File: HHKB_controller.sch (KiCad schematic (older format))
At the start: 34 parts, among them CN1 JP, CN2 PRO2, J1 USB_mini_micro_B, P1 GND, P2 D+, P3 D-, P4 VUSB, P5 PD1, P6 PD0, P7 GND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

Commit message: Add current measure pins and change pin pad size
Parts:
- added P10, P11, P9: CONN_1, keyboard_parts:PIN_1, symbol CONN_1
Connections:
- wire segments 153 -> 155
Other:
- note added: "Current measure"
- note added: "Current mesure"
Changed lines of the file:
@@
 	-1   0    0    1
 $EndComp
-Text Notes 900  3000 0    60   Italic 0
+Text Notes 900  3100 0    60   Italic 0
 USB pinouts for external connector
 Text Notes 4350 2200 0    60   Italic 0
@@
 	1    0    0    -1
 $EndComp
+$Comp
+L CONN_1 P10
+U 1 1 5485F22B
+P 2875 5450
+F 0 "P10" H 2955 5450 40  0000 L CNN
+F 1 "CONN_1" H 2875 5505 30  0001 C CNN
+F 2 "keyboard_parts:PIN_1" H 2875 5450 60  0001 C CNN
+F 3 "" H 2875 5450 60  0000 C CNN
+	1    2875 5450
+	0    -1   -1   0
+$EndComp
+$Comp
+L CONN_1 P9
+U 1 1 5485F339
+P 2775 5450
+F 0 "P9" H 2855 5450 40  0000 L CNN
+F 1 "CONN_1" H 2775 5505 30  0001 C CNN
+F 2 "keyboard_parts:PIN_1" H 2775 5450 60  0001 C CNN
+F 3 "" H 2775 5450 60  0000 C CNN
+	1    2775 5450
+	0    -1   -1   0
+$EndComp
+Text Notes 2475 5250 0    60   ~ 0
+Current mesure
+Connection ~ 2875 5600
+Connection ~ 2775 5600
+$Comp
+L CONN_1 P11
+U 1 1 54865141
+P 1150 2925
+F 0 "P11" H 1230 2925 40  0000 L CNN
+F 1 "CONN_1" H 1150 2980 30  0001 C CNN
+F 2 "keyboard_parts:PIN_1" H 1150 2925 60  0001 C CNN
+F 3 "" H 1150 2925 60  0000 C CNN
+	1    1150 2925
+	-1   0    0    1
+$EndComp
+Wire Wire Line
+	1300 2925 1375 2925
+Wire Wire Line
+	1375 2925 1375 2825
+Connection ~ 1375 2825
+Text Notes 1475 2950 0    60   ~ 0
+Current measure
 $EndSCHEMATC

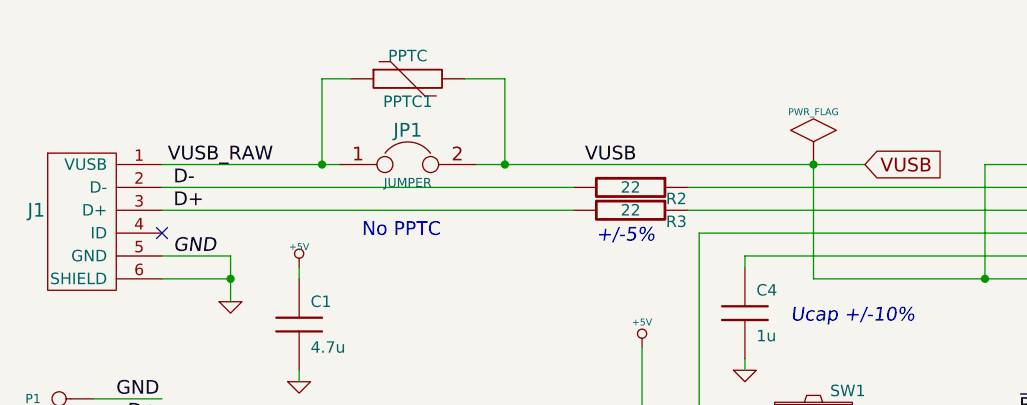
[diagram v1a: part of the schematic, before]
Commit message: Remove solder jumper for Polyfuse
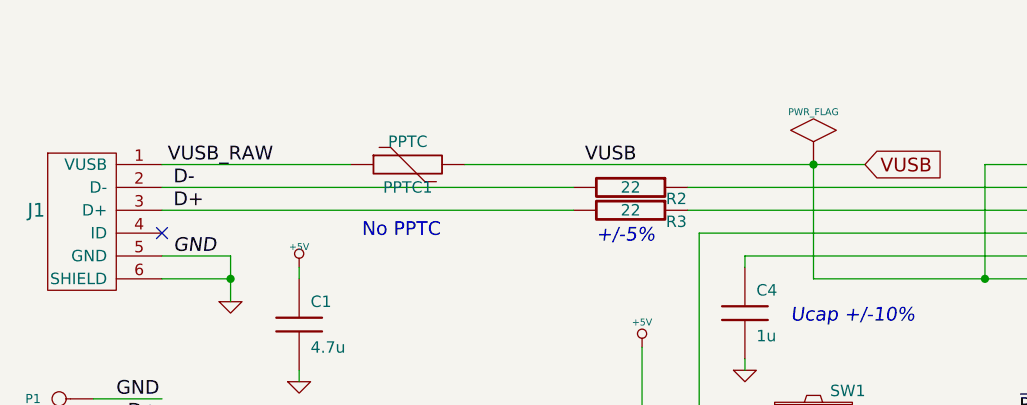
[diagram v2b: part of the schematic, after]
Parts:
- removed JP1: JUMPER, keyboard_parts:SOLDER_JUMPER_2, symbol JUMPER
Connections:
- wire segments 155 -> 151
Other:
- moved on the sheet: PPTC1
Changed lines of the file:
@@
 LIBS:keyboard_parts
 LIBS:HHKB_controller-cache
-EELAYER 24 0
+EELAYER 25 0
 EELAYER END
 $Descr A4 11693 8268
@@
 L PPTC PPTC1
 U 1 1 5417AF4F
-P 2675 1125
-F 0 "PPTC1" H 2675 1225 50  0000 C CNN
-F 1 "PPTC" H 2675 1025 50  0000 C CNN
-F 2 "keyboard_parts:PPTC_nano" V 2675 1125 60  0001 C CNN
-F 3 "" V 2675 1125 60  0000 C CNN
-	1    2675 1125
+P 2675 1500
+F 0 "PPTC1" H 2675 1600 50  0000 C CNN
+F 1 "PPTC" H 2675 1400 50  0000 C CNN
+F 2 "keyboard_parts:PPTC_nano" V 2675 1500 60  0001 C CNN
+F 3 "" V 2675 1500 60  0000 C CNN
+	1    2675 1500
 	1    0    0    1
-$EndComp
-$Comp
-L JUMPER JP1
-U 1 1 5417AF56
-P 2675 1500
-F 0 "JP1" H 2675 1650 60  0000 C CNN
-F 1 "JUMPER" H 2675 1420 40  0000 C CNN
-F 2 "keyboard_parts:SOLDER_JUMPER_2" H 2675 1500 60  0001 C CNN
-F 3 "" H 2675 1500 60  0000 C CNN
-	1    2675 1500
-	1    0    0    -1
 $EndComp
 Text Label 3450 1500 0    60   ~ 0
@@
 	5650 1700 3900 1700
 Wire Wire Line
-	1600 1500 2375 1500
-Wire Wire Line
-	2975 1500 4675 1500
-Wire Wire Line
-	2425 1125 2300 1125
-Wire Wire Line
-	2300 1125 2300 1500
-Connection ~ 2300 1500
-Wire Wire Line
-	2925 1125 3100 1125
-Wire Wire Line
-	3100 1125 3100 1500
-Connection ~ 3100 1500
+	1600 1500 2425 1500
 Wire Wire Line
 	5200 1500 5200 2000
@@
 Text Notes 1475 2950 0    60   ~ 0
 Current measure
+Wire Wire Line
+	2925 1500 4675 1500
 $EndSCHEMATC

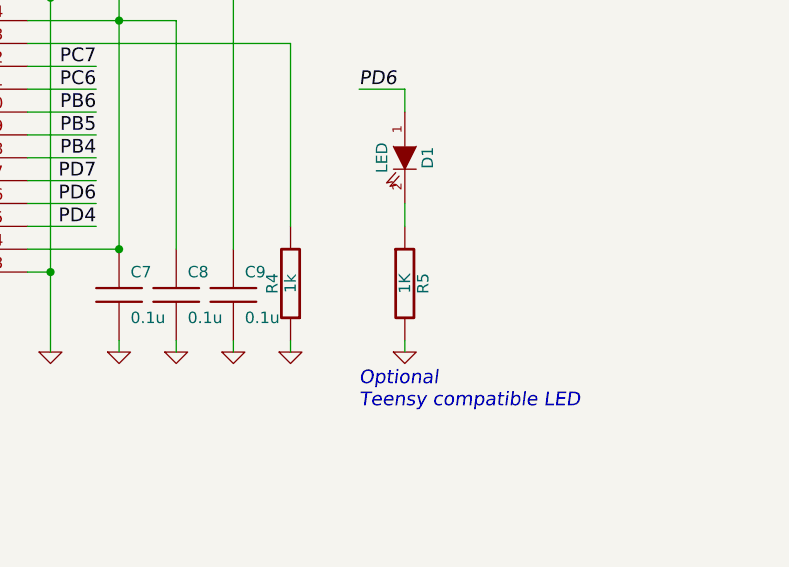
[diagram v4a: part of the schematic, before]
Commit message: Change foot print of D1 and Add D5
Change pad size of LED(D1) for proper reflow
Add D5 schottky diode for reverse polarity protection
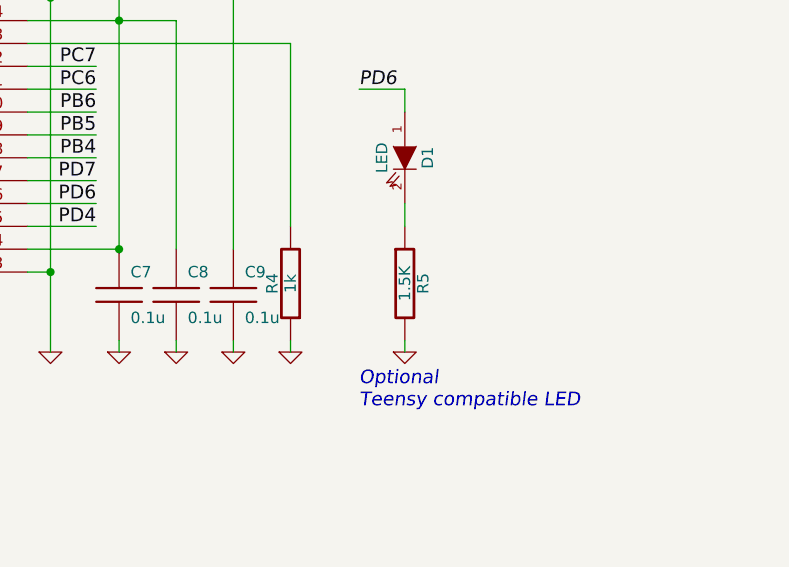
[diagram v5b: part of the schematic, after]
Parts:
- D1: footprint keyboard_parts:LED_2012_HSOL -> keyboard_parts:LED_3020_REFLOW
- R5: value 1K -> 1.5K
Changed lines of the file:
@@
 F 0 "D1" H 9450 3100 50  0000 C CNN
 F 1 "LED" H 9450 2900 50  0000 C CNN
-F 2 "keyboard_parts:LED_2012_HSOL" H 9450 3000 60  0001 C CNN
+F 2 "keyboard_parts:LED_3020_REFLOW" H 9450 3000 60  0001 C CNN
 F 3 "" H 9450 3000 60  0000 C CNN
 	1    9450 3000
@@
 P 9450 3550
 F 0 "R5" V 9530 3550 50  0000 C CNN
-F 1 "1K" V 9450 3550 50  0000 C CNN
+F 1 "1.5K" V 9450 3550 50  0000 C CNN
 F 2 "keyboard_parts:R_1608" H 9450 3550 60  0001 C CNN
 F 3 "" H 9450 3550 60  0000 C CNN
